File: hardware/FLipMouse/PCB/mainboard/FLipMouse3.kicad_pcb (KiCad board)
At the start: 2 copper layers, 61 x 32 mm, 85 parts, among them J1 SJ2-3574A, J2 SJ2-3574A, J3 M50-3900542, J4 Conn_ARM_JTAG_SWD_10, J5 Conn_02x05_Odd_Even, J6 USB_OTG, J7 Conn_01x06, Q1 BC847, Q2 BC847, Q3 BSH108, Q4 BSH108, Q5 BSH108, SW1 SW_Push, SW2 SW_Push, U1 ESP32-WROOM, U2 TSOP4838, U3 LPC11U24FBD, U4 TSR_1-2433, U5 MPXV7007GP, Y1 JA-12.000-18-DFE

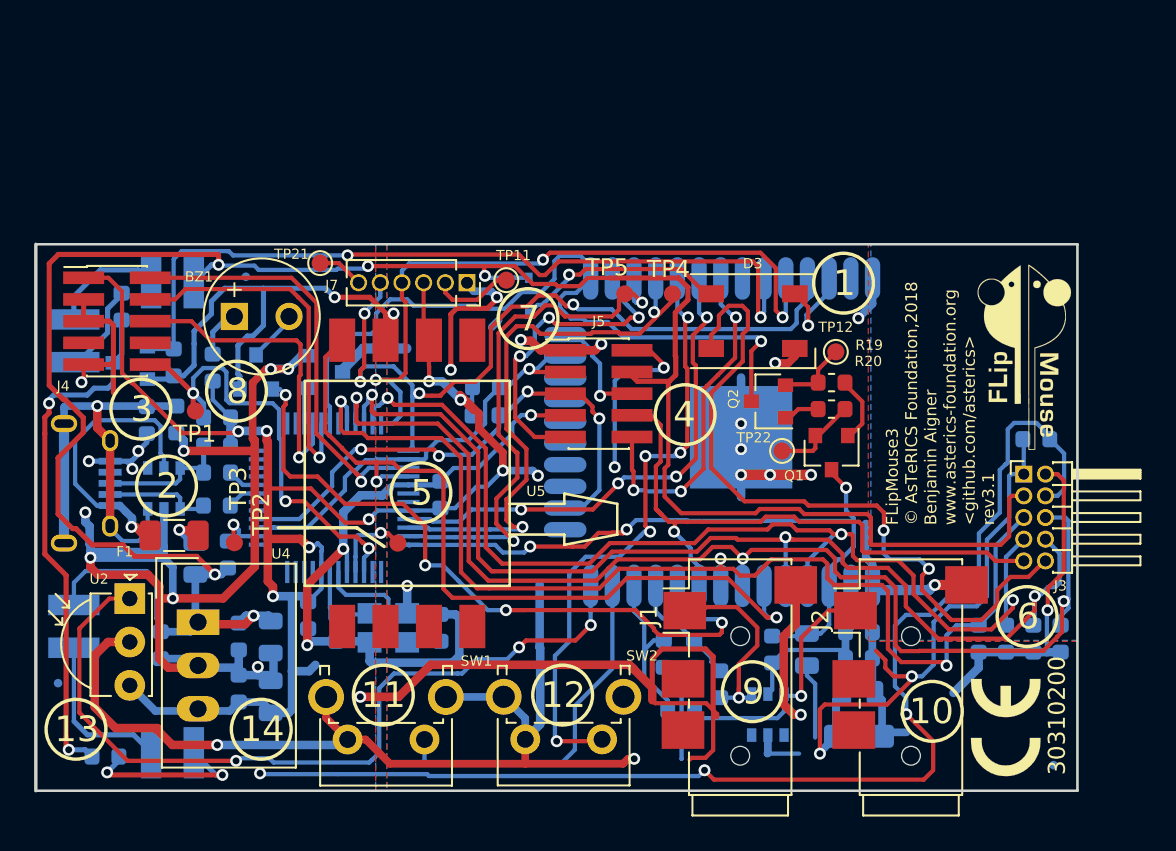
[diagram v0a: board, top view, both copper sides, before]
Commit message: Unified 3V3 (switched), according to chapter 9.4 of LPC datasheet, the high power pin doesn't deliver 3v3.
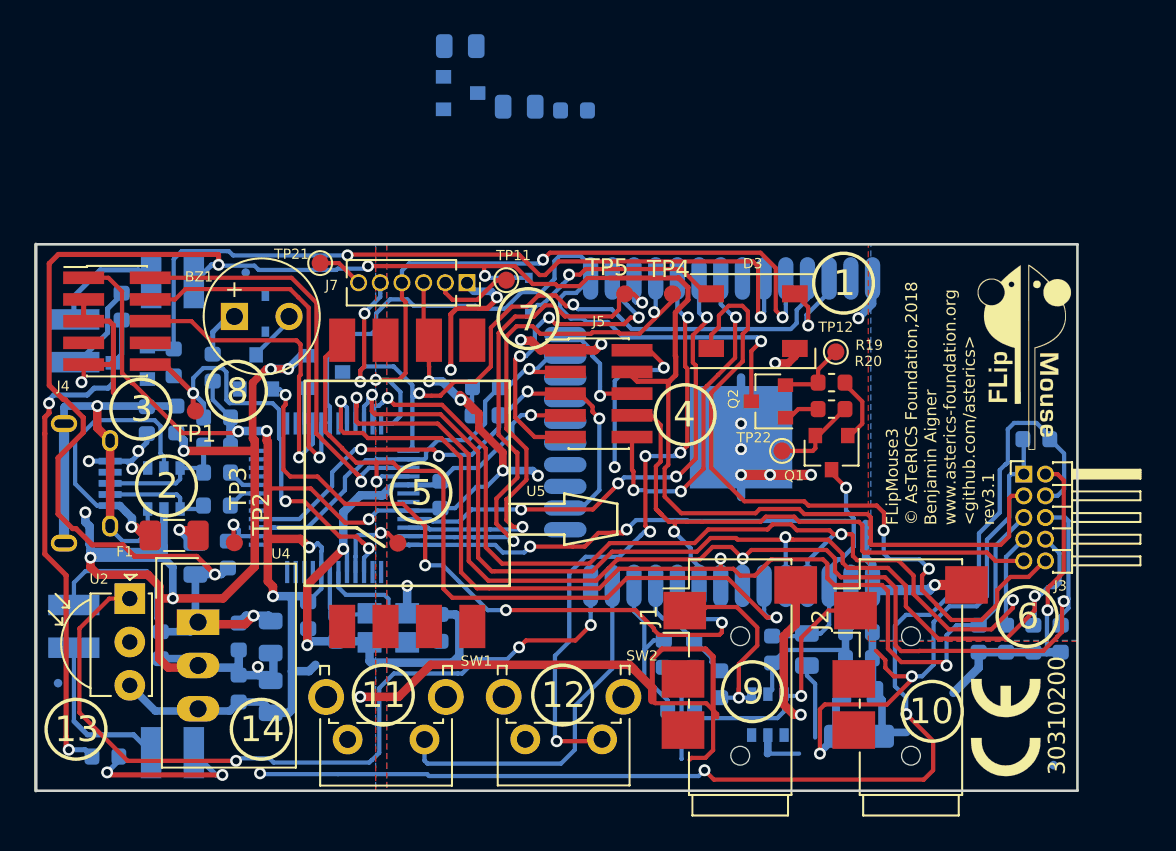
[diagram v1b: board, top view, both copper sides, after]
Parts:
- added C19: 1u, Capacitor_SMD:C_0805_2012Metric, B.Cu at (84.9, 106.4)
- added C20: 1u, Capacitor_SMD:C_0805_2012Metric, B.Cu at (88.3, 109.9)
- added D9: 1N4148WS, Diode_SMD:D_SOD-323, B.Cu at (73.4, 122.1)
- added R22: 10k, Resistor_SMD:R_0603_1608Metric, B.Cu at (91.5, 110.2)
- added U6: AP2127N-3.3, Package_TO_SOT_SMD:SOT-23, B.Cu at (84.9, 109.1)
- Q5: value BSH108 -> Si2301
- R10: value 1k5 -> 15R
- moved FID3 0.25 mm to (72.3, 119.7)
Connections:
- C10 pad 2: GNDD -> GND
- C11 pad 1: +3V3 -> VPP
- C12 pad 1: VBUS -> /VBUS_SW
- C13 pad 1: +3V3 -> VPP
- C14 pad 1: VBUS -> /VBUS_SW
- C15 pad 2: GNDD -> GND
- C16 pad 1: +3V3 -> VPP
- C17 pad 2: GNDD -> GND
- C18 pad 2: GNDD -> GND
- C3 pad 1: GNDD -> GND
- C4 pad 1: GNDD -> GND
- C7 pad 2: GNDD -> GND
- C8 pad 1: +3V3 -> VPP
- C9 pad 1: +3V3 -> VPP
- D2 pad 2: GNDD -> GND
- D3 pad 1: GNDD -> GND
- D4 pad 2: VBUS -> /VBUS_SW
- D8 pad 2: VBUS -> /VBUS_SW
- J1 pad 1: GNDD -> GND
- J2 pad 1: GNDD -> GND
- J3 pad 2: GNDD -> GND
- J3 pad 4: GND -> +3V3
- J4 pad 1: +3V3 -> VPP
- J5 pad 1: GNDD -> GND
- J7 pad 1: GNDD -> GND
- Q3 pad 2: GNDD -> GND
- Q4 pad 2: GNDD -> GND
- Q5 pad 2: GND -> VBUS
- Q5 pad 3: GNDD -> /VBUS_SW
- R12 pad 1: GNDD -> GND
- R13 pad 1: GNDD -> GND
- R14 pad 1: GNDD -> GND
- R15 pad 1: GNDD -> GND
- R16 pad 2: GNDD -> GND
- R8 pad 2: +3V3 -> VPP
- R9 pad 2: +3V3 -> VPP
- SW1 pad : GNDD -> (no net)
- SW1 pad 2: GNDD -> GND
- SW2 pad : GNDD -> (no net)
- SW2 pad 2: GNDD -> GND
- U1 pad 1: GNDD -> GND
- U1 pad 15: GNDD -> GND
- U1 pad 38: GNDD -> GND
- U1 pad 39: GNDD -> GND
- U1 pad 4: /FSR3 -> (no net)
- U1 pad 5: /FSR4 -> (no net)
- U1 pad 6: /PRESSURE -> (no net)
- U1 pad 7: /FSR2 -> (no net)
- U1 pad 8: /FSR1 -> (no net)
- U1 pad 9: /EXT1 -> (no net)
- U2 pad 2: GNDD -> GND
- U3 pad 42: (no net) -> /EXT1
- U3 pad 44: +3V3 -> VPP
- U3 pad 8: +3V3 -> VPP
- U4 pad 1: VBUS -> /VBUS_SW
- U5 pad 3: GNDD -> GND
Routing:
- net GNDD: track 186.8 -> 0.00 mm, vias 18 -> 0
- net GND: track 204.6 -> 296.7 mm, vias 18 -> 32
- added copper zone on B.Cu, net GND
- removed copper zone on B.Cu, net GNDD

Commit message: First finished PCB for prototype B (no DRC errors, everything is routed & checklist is done)
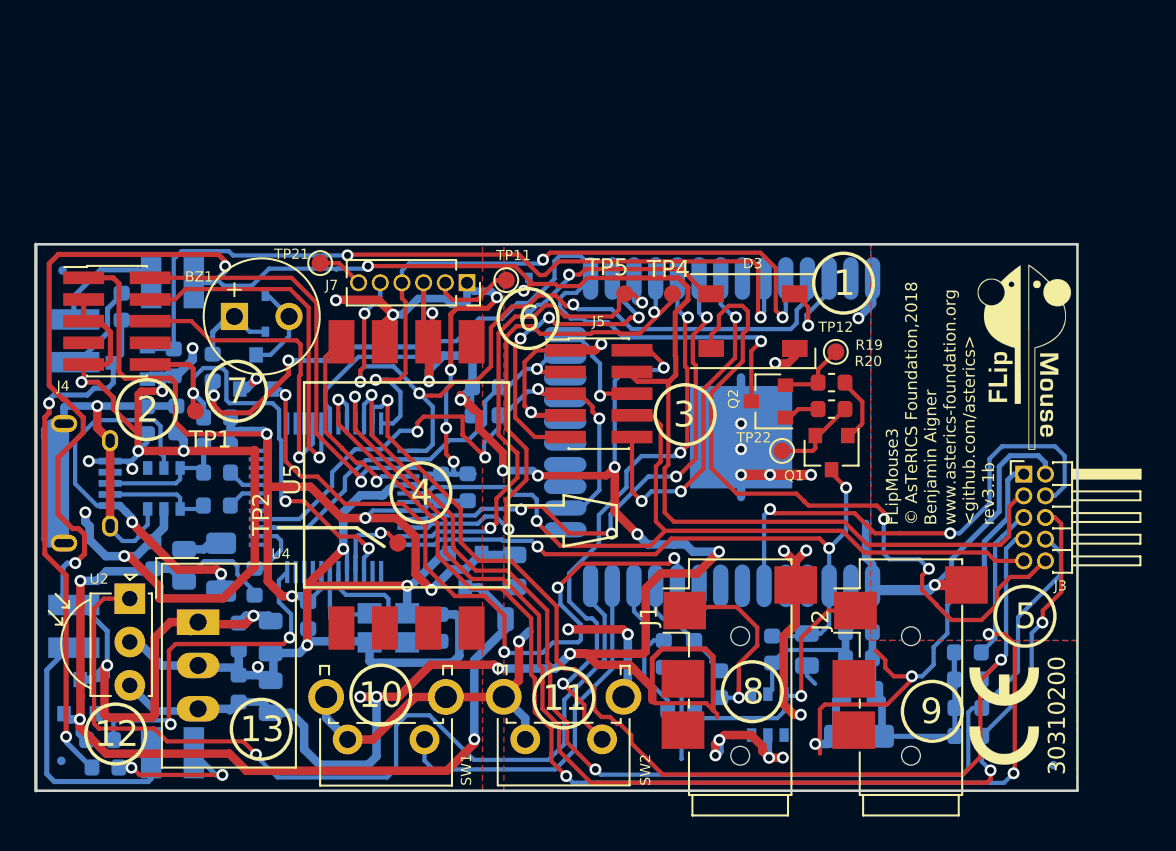
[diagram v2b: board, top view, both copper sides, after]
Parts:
- removed TP3: tp, Measurement_Points:Measurement_Point_Round-SMD-Pad_Small
- F1: moved to B.Cu
- moved R22 46.1 mm to (63.8, 147.0)
- moved C19 33.6 mm to (86.6, 139.9), turned to 180 degrees
- moved C8 33.4 mm to (85.3, 132.2), turned to 90 degrees
- moved U6 28.0 mm to (85.2, 137.1), turned to 270 degrees
- moved C18 27.2 mm to (88.0, 137.1), turned to 270 degrees
- moved Q5 23.8 mm to (62.6, 144.5), turned to 90 degrees
- moved LOGO2 23.2 mm to (118.7, 122.9), turned to 180 degrees
- moved FID3 10.7 mm to (61.6, 119.5)
- moved R13 7.85 mm to (114.6, 146.8), turned to 0 degrees
- moved R15 5.56 mm to (114.6, 145.2), turned to 0 degrees
- moved C6 5.29 mm to (66.9, 136.2), turned to 90 degrees
- moved FID2 4.55 mm to (61.5, 148.2)
- moved F1 3.32 mm to (70.8, 136.9), turned to 270 degrees
- moved R14 3.27 mm to (114.6, 143.5), turned to 0 degrees
- moved R6 2.23 mm to (72.8, 137.8)
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- renumbered C20 to C18, C18 to C20, R6 to R10, R10 to R3, R3 to R5, R5 to R6
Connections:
- C16 pad 1: VPP -> +3V3
- C9 pad 1: VPP -> +3V3
- D5 pad 2: VBUS -> /VBUS_SW
- J3 pad 3: VBUS -> /VBUS_SW
- J3 pad 4: +3V3 -> /EXT3
- J5 pad 4: VBUS -> /VBUS_SW
- U1 pad 6: (no net) -> /EXT3
- U3 pad 12: (no net) -> /ESP_POWER
- U3 pad 27: /ESP_POWER -> (no net)
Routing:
- net /VBUS_SW: track 0.00 -> 138.6 mm, vias 0 -> 6
- net VBUS: track 137.1 -> 59.8 mm, vias 5 -> 3
- net VPP: track 0.00 -> 64.0 mm, vias 0 -> 4
- net /PRESSURE: track 47.1 -> 12.1 mm, vias 2 -> 1
- net /EXT3: track 0.00 -> 30.0 mm, vias 0 -> 2
- net Net-(C5-Pad2): track 26.1 -> 52.2 mm
- net /ESP_POWER: track 2.17 -> 22.0 mm, vias 0 -> 2
- net GND: track 296.7 -> 280.3 mm, vias 32 -> 40
- net /EXT1: track 35.8 -> 48.0 mm
- net /FSR1: track 65.8 -> 75.9 mm, vias 3 -> 4
- net +3V3: track 192.2 -> 183.1 mm, vias 14 -> 17
- net Net-(D4-Pad1): track 10.1 -> 16.8 mm
- net Net-(D1-Pad5): track 16.8 -> 22.7 mm, vias 1 -> 2
- net /TSOP: track 48.6 -> 53.8 mm, vias 3 -> 1
- net /FSR4: track 64.3 -> 68.9 mm, vias 3 -> 2
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- removed copper zone on B.Cu, net +3V3
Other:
- board text added: "FLipMouse3 © AsTeRICS Foundation,2018 Benjamin Aigner www.asterics-foundation.org <github.com/asterics> rev3.1b"
- board text removed: "14"
- board text removed: "FLipMouse3 © AsTeRICS Foundation,2018 Benjamin Aigner www.asterics-foundation.org <github.com/asterics> rev3.1"
